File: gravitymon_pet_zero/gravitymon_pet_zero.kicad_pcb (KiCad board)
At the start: 2 copper layers, 123.1 x 30.7 mm, 17 parts, among them J1 Wireless Charge, J2 Wireless Charge 2, J3 Force Config, J4 Balance 1, J5 Balance 2, J6 Balance 3, SW2 SW_SPST, U1 TP-4056, U8 DS18B20

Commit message: Update pet zero
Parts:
- J2: value Wireless Charge 2 -> Wireless Charge
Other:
- board text added: "+"
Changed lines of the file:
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@@
 			)
 		)
-		(property "Value" "Wireless Charge 2"
-			(at -0.1 11.89 180)
+		(property "Value" "Wireless Charge"
+			(at 0 -8.26 180)
 			(layer "F.SilkS")
 			(effects
@@
 		(tags "Resistor Axial_DIN0204 series Axial Horizontal pin pitch 7.62mm 0.167W length 3.6mm diameter 1.6mm")
 		(property "Reference" "R3"
-			(at 3.81 1.92 270)
+			(at 3.81 0 270)
 			(layer "B.SilkS")
 			(effects
@@
 		)
 		(property "Value" "4.7k"
-			(at 3.81 -1.92 270)
-			(layer "B.Fab")
+			(at 3.81 2.6 270)
+			(layer "B.SilkS")
 			(effects
 				(font
@@
 		(tags "Resistor Axial_DIN0204 series Axial Horizontal pin pitch 7.62mm 0.167W length 3.6mm diameter 1.6mm")
 		(property "Reference" "R4"
-			(at 3.81 1.92 90)
+			(at 3.81 0 90)
 			(layer "B.SilkS")
 			(effects
@@
 		)
 		(property "Value" "220k"
-			(at 3.81 -1.92 90)
-			(layer "B.Fab")
+			(at 3.81 2.6 90)
+			(layer "B.SilkS")
 			(effects
 				(font
@@
 		(tags "Resistor Axial_DIN0204 series Axial Horizontal pin pitch 7.62mm 0.167W length 3.6mm diameter 1.6mm")
 		(property "Reference" "R1"
-			(at 3.81 1.92 90)
+			(at 3.81 0 90)
 			(layer "B.SilkS")
 			(effects
@@
 		)
 		(property "Value" "220k"
-			(at 3.81 -1.92 90)
-			(layer "B.Fab")
+			(at 4.21 2.1 90)
+			(layer "B.SilkS")
 			(effects
 				(font
@@
 		(tags "Resistor Axial_DIN0204 series Axial Horizontal pin pitch 7.62mm 0.167W length 3.6mm diameter 1.6mm")
 		(property "Reference" "R2"
-			(at 3.81 1.92 90)
+			(at 3.81 0 90)
 			(layer "B.SilkS")
 			(effects
@@
 		(property "Value" "220k"
 			(at 3.81 -1.92 90)
-			(layer "B.Fab")
+			(layer "B.SilkS")
 			(effects
 				(font
@@
 		)
 	)
+	(gr_text "+"
+		(at 165.3 83.06 0)
+		(layer "F.SilkS")
+		(effects
+			(font
+				(size 1.5 1.5)
+				(thickness 0.3)
+				(bold yes)
+			)
+			(justify left bottom)
+		)
+	)
+	(gr_text "+"
+		(at 173.3 109.26 0)
+		(layer "F.SilkS")
+		(effects
+			(font
+				(size 1.5 1.5)
+				(thickness 0.3)
+				(bold yes)
+			)
+			(justify left bottom)
+		)
+	)

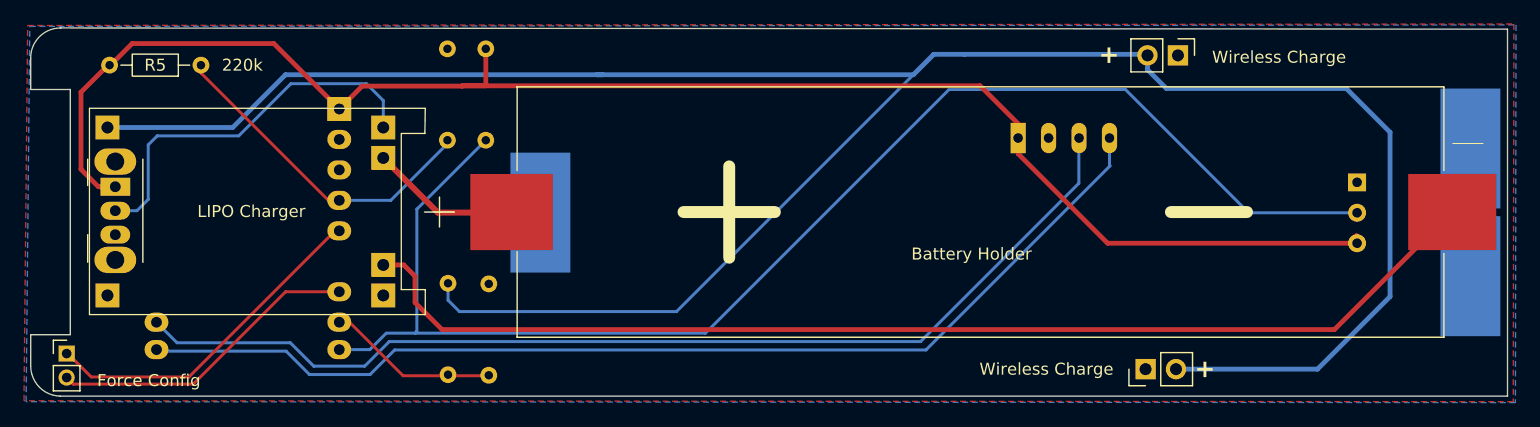
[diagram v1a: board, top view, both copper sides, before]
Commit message: Update r1 + r2 to 10k
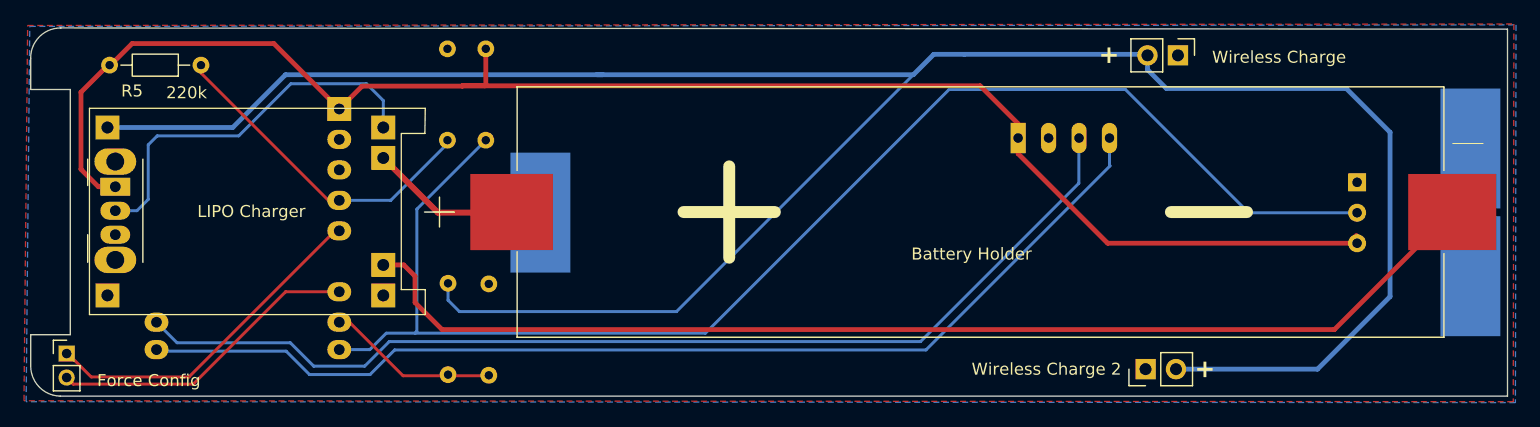
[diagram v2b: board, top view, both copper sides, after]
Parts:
- J2: value Wireless Charge -> Wireless Charge 2
- R1, R2: value 220k -> 10k
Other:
- board text added: "Gravitymon ESP32c3 Zero PET version v1.1 (c) 2025 Magnus Persson"
- board text removed: "Gravitymon ESP32c3 Zero PET version v1.0 (c) 2025 Magnus Persson"
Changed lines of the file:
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@@
 			)
 		)
-		(property "Value" "Wireless Charge"
+		(property "Value" "Wireless Charge 2"
 			(at 0 -8.26 180)
 			(layer "F.SilkS")
@@
 		(tags "Resistor Axial_DIN0204 series Axial Horizontal pin pitch 7.62mm 0.167W length 3.6mm diameter 1.6mm")
 		(property "Reference" "R5"
-			(at 3.81 0 180)
+			(at 5.75 -2.15 180)
 			(layer "F.SilkS")
 			(effects
@@
 		)
 		(property "Value" "220k"
-			(at -3.45 0 180)
+			(at 1.2 -2.3 180)
 			(layer "F.SilkS")
 			(effects
@@
 		(tags "Resistor Axial_DIN0204 series Axial Horizontal pin pitch 7.62mm 0.167W length 3.6mm diameter 1.6mm")
 		(property "Reference" "R3"
-			(at 3.81 0 270)
+			(at 7.51 2.05 270)
 			(layer "B.SilkS")
 			(effects
@@
 		)
 		(property "Value" "4.7k"
-			(at 3.81 2.6 270)
+			(at 3.81 2.15 270)
 			(layer "B.SilkS")
 			(effects
@@
 		(tags "Resistor Axial_DIN0204 series Axial Horizontal pin pitch 7.62mm 0.167W length 3.6mm diameter 1.6mm")
 		(property "Reference" "R4"
-			(at 3.81 0 90)
+			(at 0.06 2.1 90)
 			(layer "B.SilkS")
 			(effects
@@
 		)
 		(property "Value" "220k"
-			(at 3.81 2.6 90)
+			(at 3.81 2.05 90)
 			(layer "B.SilkS")
 			(effects
@@
 		(tags "Resistor Axial_DIN0204 series Axial Horizontal pin pitch 7.62mm 0.167W length 3.6mm diameter 1.6mm")
 		(property "Reference" "R1"
-			(at 3.81 0 90)
-			(layer "B.SilkS")
-			(effects
-				(font
-					(size 1 1)
-					(thickness 0.15)
-				)
-				(justify mirror)
-			)
-		)
-		(property "Value" "220k"
-			(at 4.21 2.1 90)
+			(at 7.41 2 90)
+			(layer "B.SilkS")
+			(effects
+				(font
+					(size 1 1)
+					(thickness 0.15)
+				)
+				(justify mirror)
+			)
+		)
+		(property "Value" "10k"
+			(at 3.81 2 90)
 			(layer "B.SilkS")
 			(effects
@@
 		(tags "Resistor Axial_DIN0204 series Axial Horizontal pin pitch 7.62mm 0.167W length 3.6mm diameter 1.6mm")
 		(property "Reference" "R2"
-			(at 3.81 0 90)
-			(layer "B.SilkS")
-			(effects
-				(font
-					(size 1 1)
-					(thickness 0.15)
-				)
-				(justify mirror)
-			)
-		)
-		(property "Value" "220k"
-			(at 3.81 -1.92 90)
+			(at 7.36 -2.1 90)
+			(layer "B.SilkS")
+			(effects
+				(font
+					(size 1 1)
+					(thickness 0.15)
+				)
+				(justify mirror)
+			)
+		)
+		(property "Value" "10k"
+			(at 3.16 -2.15 90)
 			(layer "B.SilkS")
 			(effects
@@
 		)
 	)
-	(gr_text "Gravitymon ESP32c3 Zero PET version v1.0\n(c) 2025 Magnus Persson"
-		(at 137.55 88.91 0)
+	(gr_text "Gravitymon ESP32c3 Zero \nPET version v1.1\n(c) 2025 Magnus Persson"
+		(at 139.3 95.11 0)
 		(layer "B.SilkS")
 		(effects
 			(font
-				(size 1 1)
-				(thickness 0.15)
+				(size 1.2 1.2)
+				(thickness 0.2)
+				(bold yes)
 			)
 			(justify mirror)

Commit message: Update gravitymon pet zero board to use 3.3V supply to components
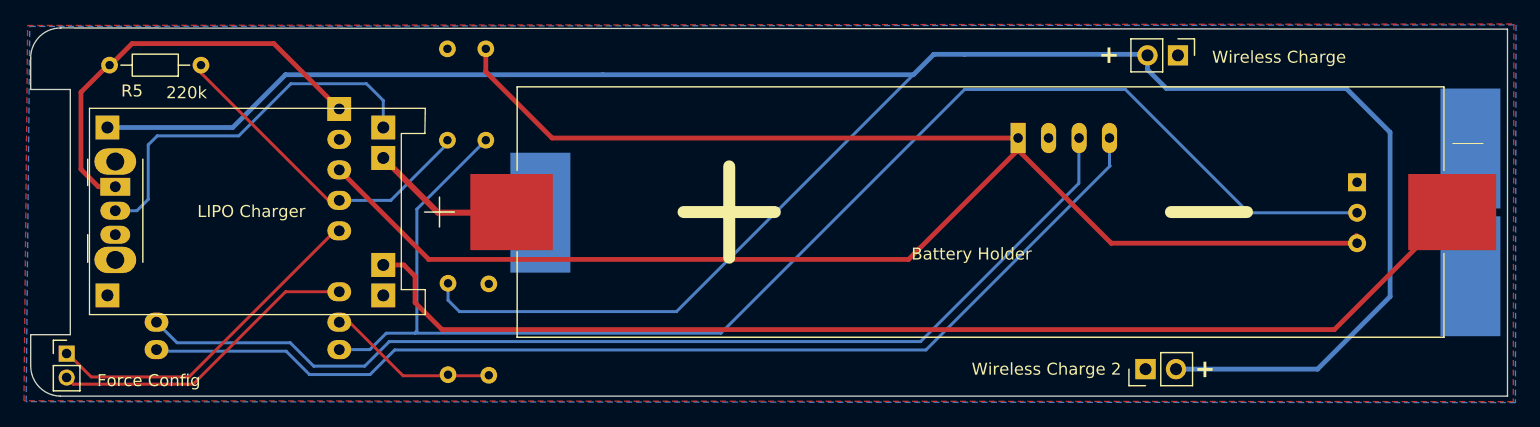
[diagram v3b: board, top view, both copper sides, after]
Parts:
- R3: value 4.7k -> 3.3k
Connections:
- R3 pad 2: VCC -> +3.3V
- U7 pad 1: VCC -> +3.3V
- U8 pad 3: VCC -> +3.3V
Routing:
- net +3.3V: track 0.00 -> 145.8 mm
- net VCC: track 133.2 -> 35.4 mm
- net /CHARGE-5V: track 196.2 -> 195.7 mm
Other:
- board text added: "Gravitymon ESP32c3 Zero PET version v1.2 (c) 2025 Magnus Persson"
- board text removed: "Gravitymon ESP32c3 Zero PET version v1.1 (c) 2025 Magnus Persson"
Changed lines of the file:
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@@
 		(tags "Resistor Axial_DIN0204 series Axial Horizontal pin pitch 7.62mm 0.167W length 3.6mm diameter 1.6mm")
 		(property "Reference" "R3"
-			(at 7.51 2.05 270)
-			(layer "B.SilkS")
-			(effects
-				(font
-					(size 1 1)
-					(thickness 0.15)
-				)
-				(justify mirror)
-			)
-		)
-		(property "Value" "4.7k"
-			(at 3.81 2.15 270)
+			(at 1.31 1.95 270)
+			(layer "B.SilkS")
+			(effects
+				(font
+					(size 1 1)
+					(thickness 0.15)
+				)
+				(justify mirror)
+			)
+		)
+		(property "Value" "3.3k"
+			(at 4.51 1.95 270)
 			(layer "B.SilkS")
 			(effects
@@
 			(layers "*.Cu" "*.Mask")
 			(remove_unused_layers no)
-			(net 1 "VCC")
+			(net 9 "+3.3V")
 			(pintype "passive")
 		)
@@
 			)
 		)
-		(fp_text user "5V"
+		(fp_text user "3.3V"
 			(at -3.175 8.255 90)
 			(unlocked yes)
@@
 			(layers "*.Cu" "*.Mask")
 			(remove_unused_layers no)
-			(net 1 "VCC")
+			(net 9 "+3.3V")
 			(pinfunction "VCC")
 			(pintype "power_in")
@@
 		(tags "Resistor Axial_DIN0204 series Axial Horizontal pin pitch 7.62mm 0.167W length 3.6mm diameter 1.6mm")
 		(property "Reference" "R4"
-			(at 0.06 2.1 90)
+			(at 6.81 2 90)
 			(layer "B.SilkS")
 			(effects
@@
 		)
 		(property "Value" "220k"
-			(at 3.81 2.05 90)
+			(at 3.21 2.15 90)
 			(layer "B.SilkS")
 			(effects
@@
 			(layers "*.Cu" "*.Mask")
 			(remove_unused_layers no)
-			(net 1 "VCC")
+			(net 9 "+3.3V")
 			(pinfunction "V_{DD}")
 			(pintype "power_in")
@@
 		(tags "Resistor Axial_DIN0204 series Axial Horizontal pin pitch 7.62mm 0.167W length 3.6mm diameter 1.6mm")
 		(property "Reference" "R1"
-			(at 7.41 2 90)
+			(at 2.76 2 90)
 			(layer "B.SilkS")
 			(effects
@@
 		)
 		(property "Value" "10k"
-			(at 3.81 2 90)
+			(at 6.16 2 90)
 			(layer "B.SilkS")
 			(effects
@@
 		(tags "Resistor Axial_DIN0204 series Axial Horizontal pin pitch 7.62mm 0.167W length 3.6mm diameter 1.6mm")
 		(property "Reference" "R2"
-			(at 7.36 -2.1 90)
+			(at 2.56 -2.2 90)
 			(layer "B.SilkS")
 			(effects
@@
 		)
 		(property "Value" "10k"
-			(at 3.16 -2.15 90)
+			(at 6.11 -2.15 90)
 			(layer "B.SilkS")
 			(effects
@@
 		)
 	)
-	(gr_text "Gravitymon ESP32c3 Zero \nPET version v1.1\n(c) 2025 Magnus Persson"
+	(gr_text "Gravitymon ESP32c3 Zero \nPET version v1.2\n(c) 2025 Magnus Persson"
 		(at 139.3 95.11 0)
 		(layer "B.SilkS")
@@
 	)
 	(segment
-		(start 114.2 84.71)
-		(end 114.2 81.7)
-		(width 0.4)
-		(layer "F.Cu")
-		(net 1)
-	)
-	(segment
 		(start 82.75 83.01)
 		(end 82.96 83.01)
@@
 	)
 	(segment
-		(start 103.8866 84.81)
-		(end 112.2252 84.81)
-		(width 0.4)
-		(layer "F.Cu")
-		(net 1)
-	)
-	(segment
-		(start 158.5854 89.1386)
-		(end 158.5854 90.4454)
-		(width 0.4)
-		(layer "F.Cu")
-		(net 1)
-	)
-	(segment
-		(start 114.1248 84.7852)
-		(end 114.2 84.71)
-		(width 0.4)
-		(layer "F.Cu")
-		(net 1)
-	)
-	(segment
-		(start 101.981 86.7156)
-		(end 103.8866 84.81)
-		(width 0.4)
-		(layer "F.Cu")
-		(net 1)
-	)
-	(segment
-		(start 158.5854 87.9454)
-		(end 158.5854 89.1386)
-		(width 0.4)
-		(layer "F.Cu")
-		(net 1)
-	)
-	(segment
-		(start 186.6382 97.41)
-		(end 186.7916 97.2566)
-		(width 0.4)
-		(layer "F.Cu")
-		(net 1)
-	)
-	(segment
-		(start 112.25 84.7852)
-		(end 155.4252 84.7852)
-		(width 0.4)
-		(layer "F.Cu")
-		(net 1)
-	)
-	(segment
-		(start 166.05 97.91)
-		(end 186.85 97.91)
-		(width 0.4)
-		(layer "F.Cu")
-		(net 1)
-	)
-	(segment
-		(start 112.2252 84.81)
-		(end 112.25 84.7852)
-		(width 0.4)
-		(layer "F.Cu")
-		(net 1)
-	)
-	(segment
 		(start 82.96 83.01)
 		(end 84.71 81.26)
@@
 	)
 	(segment
-		(start 112.25 84.7852)
-		(end 114.1248 84.7852)
-		(width 0.4)
-		(layer "F.Cu")
-		(net 1)
-	)
-	(segment
 		(start 80.4418 91.7448)
 		(end 80.4418 85.3182)
@@
 	)
 	(segment
-		(start 155.4252 84.7852)
-		(end 158.5854 87.9454)
-		(width 0.4)
-		(layer "F.Cu")
-		(net 1)
-	)
-	(segment
 		(start 83.3054 93.1992)
 		(end 81.8962 93.1992)
@@
 		(start 80.4418 85.3182)
 		(end 82.75 83.01)
-		(width 0.4)
-		(layer "F.Cu")
-		(net 1)
-	)
-	(segment
-		(start 158.5854 90.4454)
-		(end 166.05 97.91)
 		(width 0.4)
 		(layer "F.Cu")
@@
 	)
 	(segment
+		(start 108.3 105.41)
+		(end 133.8 105.41)
+		(width 0.25)
+		(layer "B.Cu")
+		(net 8)
+	)
+	(segment
+		(start 108.45 95.07)
+		(end 108.45 105.26)
+		(width 0.25)
+		(layer "B.Cu")
+		(net 8)
+	)
+	(segment
+		(start 105.9 105.41)
+		(end 104.5284 106.7816)
+		(width 0.25)
+		(layer "B.Cu")
+		(net 8)
+	)
+	(segment
 		(start 167.53 85.09)
 		(end 177.81 95.37)
@@
 	)
 	(segment
+		(start 154.12 85.09)
+		(end 167.53 85.09)
+		(width 0.25)
+		(layer "B.Cu")
+		(net 8)
+	)
+	(segment
+		(start 104.5284 106.7816)
+		(end 101.981 106.7816)
+		(width 0.25)
+		(layer "B.Cu")
+		(net 8)
+	)
+	(segment
+		(start 108.45 105.26)
+		(end 108.3 105.41)
+		(width 0.25)
+		(layer "B.Cu")
+		(net 8)
+	)
+	(segment
+		(start 114.2 89.32)
+		(end 108.45 95.07)
+		(width 0.25)
+		(layer "B.Cu")
+		(net 8)
+	)
+	(segment
+		(start 133.8 105.41)
+		(end 154.12 85.09)
+		(width 0.25)
+		(layer "B.Cu")
+		(net 8)
+	)
+	(segment
 		(start 177.81 95.37)
 		(end 186.85 95.37)
@@
 	)
 	(segment
-		(start 108.45 95.07)
-		(end 108.45 105.26)
-		(width 0.25)
-		(layer "B.Cu")
-		(net 8)
-	)
-	(segment
-		(start 105.9 105.41)
-		(end 104.5284 106.7816)
-		(width 0.25)
-		(layer "B.Cu")
-		(net 8)
-	)
-	(segment
-		(start 104.5284 106.7816)
-		(end 101.981 106.7816)
-		(width 0.25)
-		(layer "B.Cu")
-		(net 8)
-	)
-	(segment
-		(start 108.45 105.26)
-		(end 108.3 105.41)
-		(width 0.25)
-		(layer "B.Cu")
-		(net 8)
-	)
-	(segment
-		(start 108.3 105.41)
-		(end 132.5118 105.41)
-		(width 0.25)
-		(layer "B.Cu")
-		(net 8)
-	)
-	(segment
-		(start 114.2 89.32)
-		(end 108.45 95.07)
-		(width 0.25)
-		(layer "B.Cu")
-		(net 8)
-	)
-	(segment
-		(start 152.8318 85.09)
-		(end 167.53 85.09)
-		(width 0.25)
-		(layer "B.Cu")
-		(net 8)
-	)
-	(segment
-		(start 132.5118 105.41)
-		(end 152.8318 85.09)
-		(width 0.25)
-		(layer "B.Cu")
-		(net 8)
-	)
-	(segment
 		(start 108.3 105.41)
 		(end 105.9 105.41)
@@
 	)
 	(segment
+		(start 109.4454 99.26)
+		(end 149.45 99.26)
+		(width 0.4)
+		(layer "F.Cu")
+		(net 9)
+	)
+	(segment
+		(start 158.5854 90.1246)
+		(end 158.5854 89.1386)
+		(width 0.4)
+		(layer "F.Cu")
+		(net 9)
+	)
+	(segment
+		(start 101.981 91.7956)
+		(end 109.4454 99.26)
+		(width 0.4)
+		(layer "F.Cu")
+		(net 9)
+	)
+	(segment
+		(start 166.35 97.91)
+		(end 186.85 97.91)
+		(width 0.4)
+		(layer "F.Cu")
+		(net 9)
+	)
+	(segment
+		(start 186.6382 97.41)
+		(end 186.7916 97.2566)
+		(width 0.4)
+		(layer "F.Cu")
+		(net 9)
+	)
+	(segment
+		(start 119.7286 89.1386)
+		(end 158.5854 89.1386)
+		(width 0.4)
+		(layer "F.Cu")
+		(net 9)
+	)
+	(segment
+		(start 158.5854 90.1454)
+		(end 166.35 97.91)
+		(width 0.4)
+		(layer "F.Cu")
+		(net 9)
+	)
+	(segment
+		(start 158.5854 89.1386)
+		(end 158.5854 90.1454)
+		(width 0.4)
+		(layer "F.Cu")
+		(net 9)
+	)
+	(segment
+		(start 149.45 99.26)
+		(end 158.5854 90.1246)
+		(width 0.4)
+		(layer "F.Cu")
+		(net 9)
+	)
+	(segment
+		(start 114.2 83.61)
+		(end 119.7286 89.1386)
+		(width 0.4)
+		(layer "F.Cu")
+		(net 9)
+	)
+	(segment
+		(start 114.2 81.7)
+		(end 114.2 83.61)
+		(width 0.4)
+		(layer "F.Cu")
+		(net 9)
+	)
+	(segment
 		(start 90.45 83.71)
 		(end 101.1 94.36)
@@
 		(layer "B.Cu")
 		(net 15)
-	)
-	(segment
-		(start 123.45 83.86)
-		(end 123.95 83.86)
-		(width 0.4)
-		(layer "B.Cu")
-		(net 15)
